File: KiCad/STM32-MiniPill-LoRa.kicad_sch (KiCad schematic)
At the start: 9 parts, among them U1 STM32L051C8Tx, U2 RFM95W-868S2

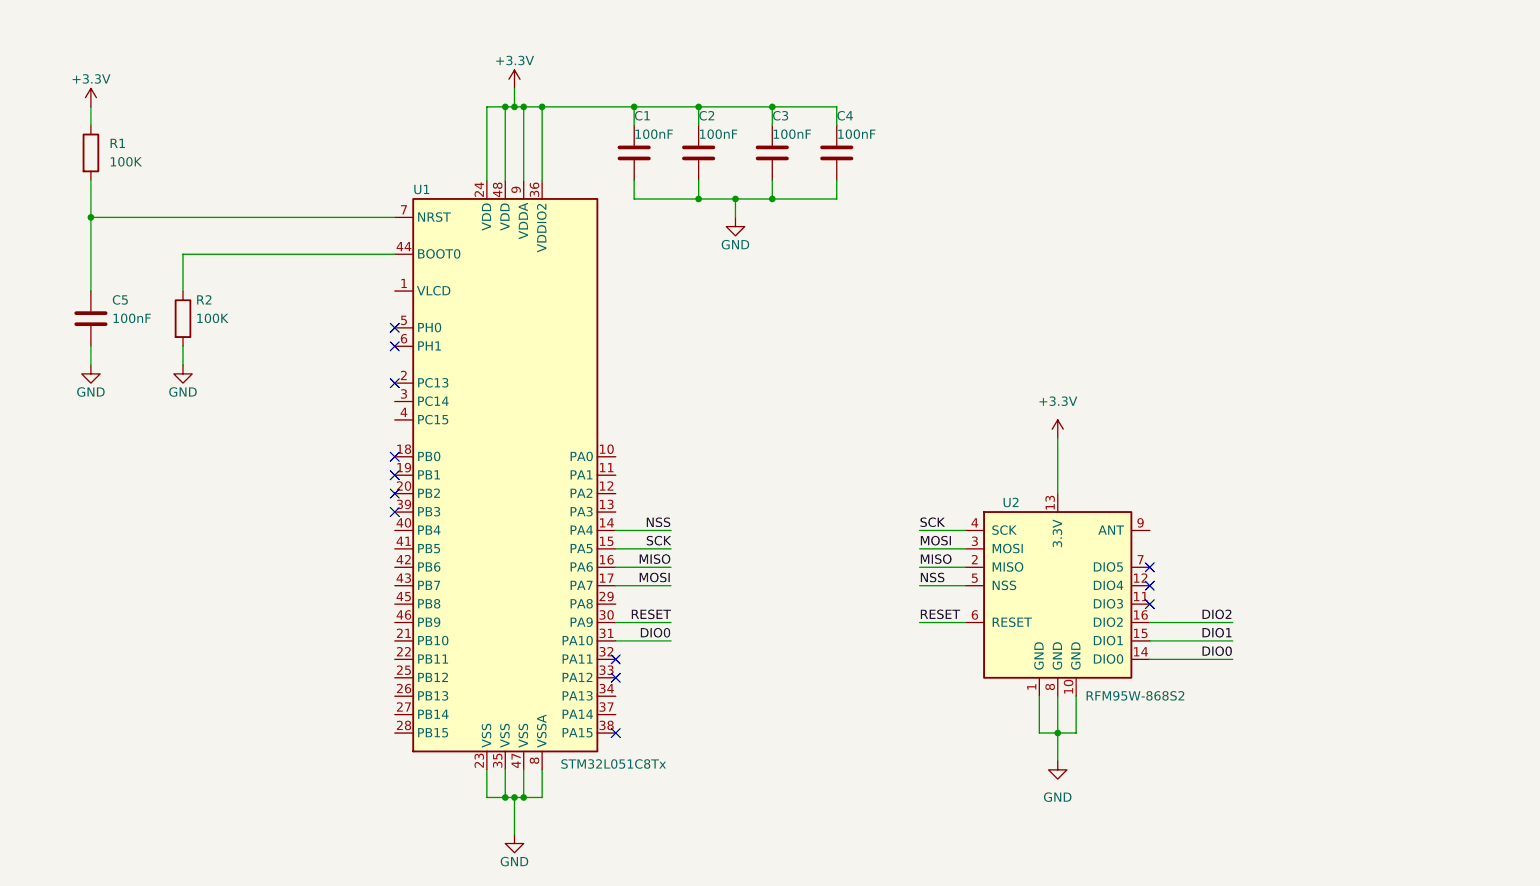
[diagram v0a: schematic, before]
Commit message: adding ST-Link Connector
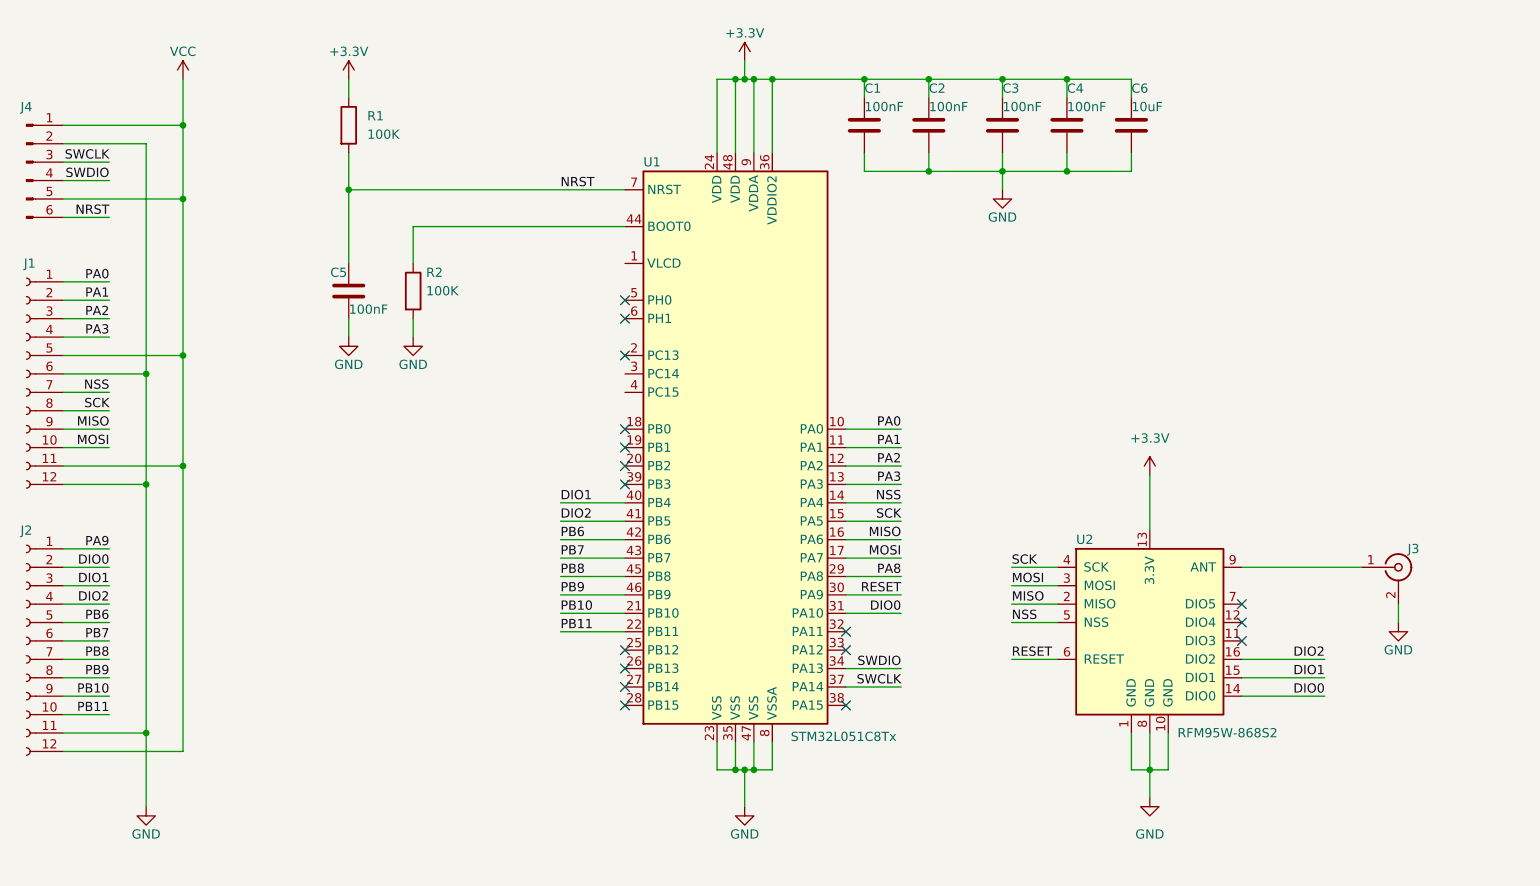
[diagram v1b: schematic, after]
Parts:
- added C6: 10uF, Capacitor_SMD:C_0805_2012Metric, symbol Device:C
- added J1, J2: Conn_01x12_Female, Connector_PinSocket_2.54mm:PinSocket_1x12_P2.54mm_Vertical, symbol Connector:Conn_01x12_Female
- added J3: Conn_Coaxial, Connector_Coaxial:SMA_Molex_73251-1153_EdgeMount_Horizontal, symbol Connector:Conn_Coaxial
- added J4: Conn_01x06_Male, Connector_PinHeader_2.54mm:PinHeader_1x06_P2.54mm_Horizontal, symbol Connector:Conn_01x06_Male
- U2: footprint (none) -> RF_Module:HOPERF_RFM9XW_SMD
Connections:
- net +3.3V: now also C6.1
- net DIO0: now also J2.2 (Pin_2)
- net DIO1: now also U1.40 (PB4), J2.3 (Pin_3)
- net DIO2: now also U1.41 (PB5), J2.4 (Pin_4)
- net GND: now also C6.2, J1.12 (Pin_12), J1.6 (Pin_6), J2.11 (Pin_11), J3.2 (Ext), J4.2 (Pin_2)
- net MISO: now also J1.9 (Pin_9)
- net MOSI: now also J1.10 (Pin_10)
- net NSS: now also J1.7 (Pin_7)
- net SCK: now also J1.8 (Pin_8)
- net at U2.9 (ANT): now also J3.1 (In)
- net PA0: now reaches U1.10 (PA0)
- net PA0: now also J1.1 (Pin_1)
- net PA1: now reaches U1.11 (PA1)
- net PA1: now also J1.2 (Pin_2)
- net PA2: now reaches U1.12 (PA2)
- net PA2: now also J1.3 (Pin_3)
- net PA3: now reaches U1.13 (PA3)
- net PA3: now also J1.4 (Pin_4)
- net PB10: now reaches U1.21 (PB10)
- net PB10: now also J2.9 (Pin_9)
- net PB11: now reaches U1.22 (PB11)
- net PB11: now also J2.10 (Pin_10)
- net PA8: now reaches U1.29 (PA8)
- net SWDIO: now reaches U1.34 (PA13)
- net SWDIO: now also J4.4 (Pin_4)
- net SWCLK: now reaches U1.37 (PA14)
- net SWCLK: now also J4.3 (Pin_3)
- net PB6: now reaches U1.42 (PB6)
- net PB6: now also J2.5 (Pin_5)
- net PB7: now reaches U1.43 (PB7)
- net PB7: now also J2.6 (Pin_6)
- net PB8: now reaches U1.45 (PB8)
- net PB8: now also J2.7 (Pin_7)
- net PB9: now reaches U1.46 (PB9)
- net PB9: now also J2.8 (Pin_8)
- net NRST: now reaches C5.1, R1.2, U1.7 (NRST)
- net NRST: now also J4.6 (Pin_6)
- new net PA9: J2.1 (Pin_1)
- new net VCC: J1.11 (Pin_11), J1.5 (Pin_5), J2.12 (Pin_12), J4.1 (Pin_1), J4.5 (Pin_5)
- no-connect marks 13 -> 17
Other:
- moved on the sheet: C1, C2, C3, C4, C5, R1, R2, U1, U2

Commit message: adding 3D Models of SMA Molex Connector
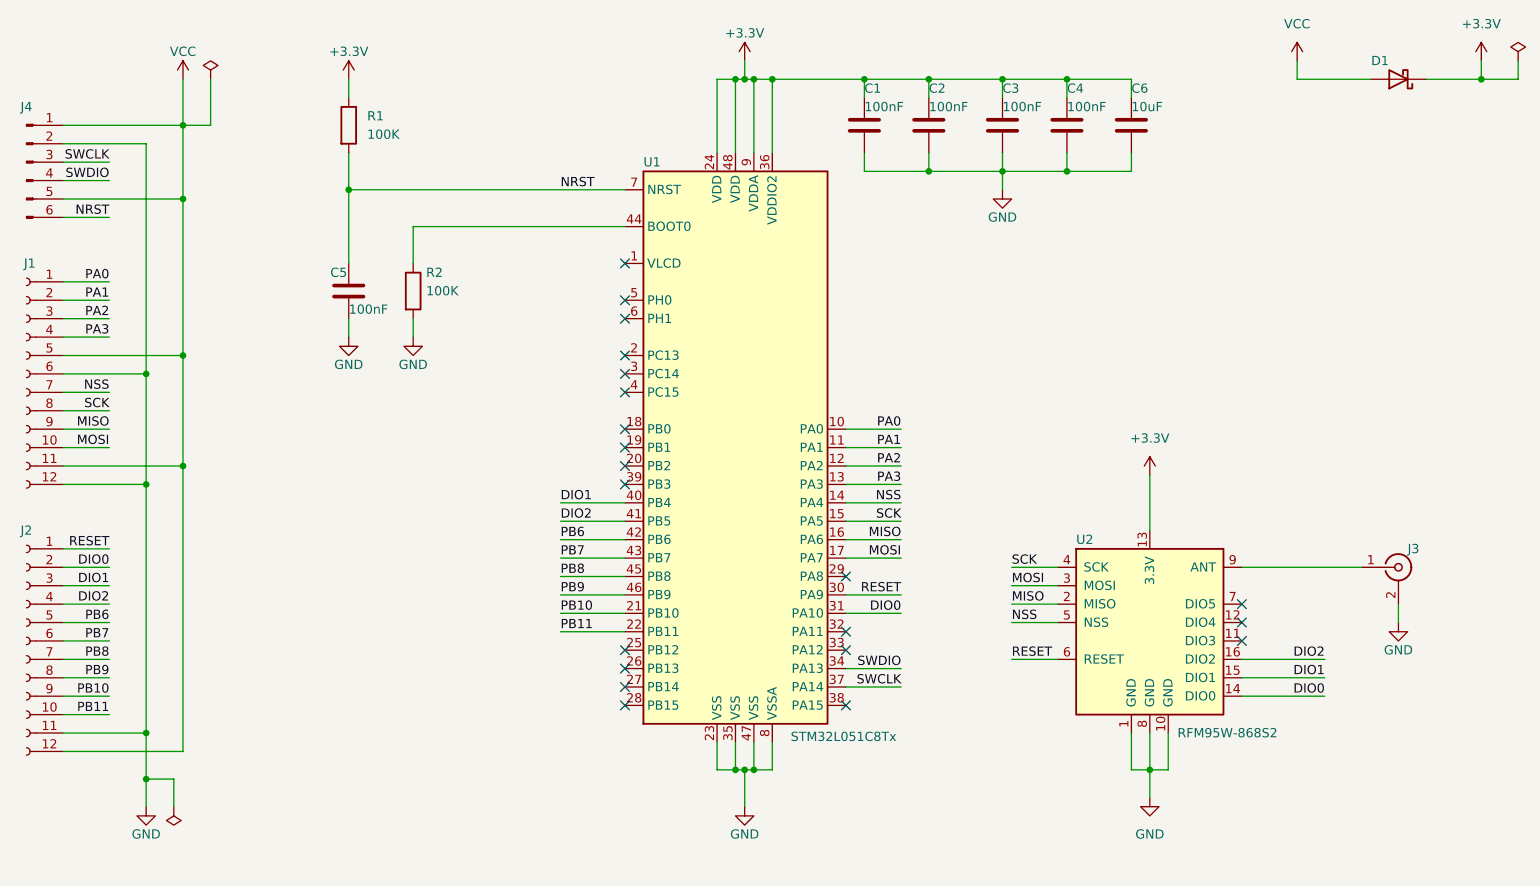
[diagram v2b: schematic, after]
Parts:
- added D1: D, Diode_SMD:D_1206_3216Metric, symbol Device:D_Schottky
- J1, J2: symbol Connector:Conn_01x12_Female -> Connector:Conn_01x12_Socket
- J4: symbol Connector:Conn_01x06_Male -> Connector:Conn_01x06_Pin
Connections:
- net PA9 is gone; now on net RESET: J2.1 (Pin_1)
- net +3.3V: now also D1.1 (K)
- net VCC: now also D1.2 (A)
- net PA8: no longer names the net of U1.29 (PA8)
- no-connect marks 17 -> 21

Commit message: fist order
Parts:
- removed D1: D, Diode_SMD:D_1206_3216Metric, symbol Device:D_Schottky
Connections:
- net +3.3V is gone; now on net VCC: C1.1, C2.1, C3.1, C4.1, C6.1, R1.1, U1.24 (VDD), U1.36 (VDDIO2), U1.48 (VDD), U1.9 (VDDA), U2.13 (3.3V)
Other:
- moved on the sheet: J4
